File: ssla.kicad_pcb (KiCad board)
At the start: 4 copper layers, 71 x 43 mm, 56 parts, among them J101 USB_C_Receptacle_USB2.0_14P, J102 Conn_02x10_Odd_Even, J103 Conn_02x10_Odd_Even, J104 Conn_02x10_Odd_Even, J105 Conn_02x10_Odd_Even, U101 TLV75533PDRV, U102 TLV75512PDRV, U103 USBLC6-2P6, U104 CY7C68013A-56LTX, U105 ICE40HX8K-BG121, Y101 24 MHz

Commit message: 0 unrouted
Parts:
- added C15: 0.1u, Capacitor_SMD:C_0402_1005Metric, F.Cu at (136.3, 82.7)
- added C28: 0.1u, Capacitor_SMD:C_0402_1005Metric, B.Cu at (156.0, 84.8)
- added C31: 0.1u, Capacitor_SMD:C_0402_1005Metric, B.Cu at (163.1, 84.2)
- added C36: 0.1u, Capacitor_SMD:C_0402_1005Metric, B.Cu at (153.5, 83.6)
- added D1: D_TVS_Small, Diode_SMD:D_SOD-923, B.Cu at (190.9, 90.3)
- added D10: D_TVS_Small, Diode_SMD:D_SOD-923, B.Cu at (188.3, 97.9)
- added D11: D_TVS_Small, Diode_SMD:D_SOD-923, B.Cu at (183.3, 97.9)
- added D12: D_TVS_Small, Diode_SMD:D_SOD-923, B.Cu at (180.7, 97.9)
- added D13: D_TVS_Small, Diode_SMD:D_SOD-923, B.Cu at (178.2, 97.9)
- added D14: D_TVS_Small, Diode_SMD:D_SOD-923, B.Cu at (175.6, 97.9)
- added D15: D_TVS_Small, Diode_SMD:D_SOD-923, B.Cu at (170.6, 97.9)
- added D16: D_TVS_Small, Diode_SMD:D_SOD-923, B.Cu at (168.0, 97.9)
- added D17: D_TVS_Small, Diode_SMD:D_SOD-923, B.Cu at (155.9, 90.3)
- added D18: D_TVS_Small, Diode_SMD:D_SOD-923, B.Cu at (153.3, 90.3)
- added D19: D_TVS_Small, Diode_SMD:D_SOD-923, B.Cu at (148.3, 90.3)
- added D2: D_TVS_Small, Diode_SMD:D_SOD-923, B.Cu at (188.3, 90.3)
- added D20: D_TVS_Small, Diode_SMD:D_SOD-923, B.Cu at (145.7, 90.3)
- added D21: D_TVS_Small, Diode_SMD:D_SOD-923, B.Cu at (143.2, 90.3)
- added D22: D_TVS_Small, Diode_SMD:D_SOD-923, B.Cu at (140.6, 90.3)
- added D23: D_TVS_Small, Diode_SMD:D_SOD-923, B.Cu at (135.6, 90.3)
- added D24: D_TVS_Small, Diode_SMD:D_SOD-923, B.Cu at (133.0, 90.3)
- added D25: D_TVS_Small, Diode_SMD:D_SOD-923, B.Cu at (155.9, 97.9)
- added D26: D_TVS_Small, Diode_SMD:D_SOD-923, B.Cu at (153.3, 97.9)
- added D27: D_TVS_Small, Diode_SMD:D_SOD-923, B.Cu at (148.3, 97.9)
- added D28: D_TVS_Small, Diode_SMD:D_SOD-923, B.Cu at (145.7, 97.9)
- added D29: D_TVS_Small, Diode_SMD:D_SOD-923, B.Cu at (143.2, 97.9)
- added D3: D_TVS_Small, Diode_SMD:D_SOD-923, B.Cu at (183.3, 90.3)
- added D30: D_TVS_Small, Diode_SMD:D_SOD-923, B.Cu at (140.6, 97.9)
- added D31: D_TVS_Small, Diode_SMD:D_SOD-923, B.Cu at (135.6, 97.9)
- added D32: D_TVS_Small, Diode_SMD:D_SOD-923, B.Cu at (133.0, 97.9)
- added D33: D_TVS_Small, Diode_SMD:D_SOD-923, B.Cu at (155.1, 62.1)
- added D34: D_TVS_Small, Diode_SMD:D_SOD-923, B.Cu at (152.5, 62.1)
- added D35: D_TVS_Small, Diode_SMD:D_SOD-923, B.Cu at (147.5, 62.1)
- added D36: D_TVS_Small, Diode_SMD:D_SOD-923, B.Cu at (144.9, 62.1)
- added D37: D_TVS_Small, Diode_SMD:D_SOD-923, B.Cu at (142.4, 62.1)
- added D38: D_TVS_Small, Diode_SMD:D_SOD-923, B.Cu at (139.8, 62.1)
- added D39: D_TVS_Small, Diode_SMD:D_SOD-923, B.Cu at (134.8, 62.1)
- added D4: D_TVS_Small, Diode_SMD:D_SOD-923, B.Cu at (180.7, 90.3)
- added D40: D_TVS_Small, Diode_SMD:D_SOD-923, B.Cu at (132.2, 62.1)
- added D41: D_TVS_Small, Diode_SMD:D_SOD-923, B.Cu at (155.1, 69.7)
- added D42: D_TVS_Small, Diode_SMD:D_SOD-923, B.Cu at (152.5, 69.7)
- added D43: D_TVS_Small, Diode_SMD:D_SOD-923, B.Cu at (147.5, 69.7)
- added D44: D_TVS_Small, Diode_SMD:D_SOD-923, B.Cu at (144.9, 69.7)
- added D45: D_TVS_Small, Diode_SMD:D_SOD-923, B.Cu at (142.4, 69.7)
- added D46: D_TVS_Small, Diode_SMD:D_SOD-923, B.Cu at (139.8, 69.7)
- added D47: D_TVS_Small, Diode_SMD:D_SOD-923, B.Cu at (134.8, 69.7)
- added D48: D_TVS_Small, Diode_SMD:D_SOD-923, B.Cu at (132.2, 69.7)
- added D49: D_TVS_Small, Diode_SMD:D_SOD-923, B.Cu at (190.1, 62.1)
- added D5: D_TVS_Small, Diode_SMD:D_SOD-923, B.Cu at (178.2, 90.3)
- added D50: D_TVS_Small, Diode_SMD:D_SOD-923, B.Cu at (187.5, 62.1)
- added D51: D_TVS_Small, Diode_SMD:D_SOD-923, B.Cu at (182.5, 62.1)
- added D52: D_TVS_Small, Diode_SMD:D_SOD-923, B.Cu at (179.9, 62.1)
- added D53: D_TVS_Small, Diode_SMD:D_SOD-923, B.Cu at (177.4, 62.1)
- added D54: D_TVS_Small, Diode_SMD:D_SOD-923, B.Cu at (174.8, 62.1)
- added D55: D_TVS_Small, Diode_SMD:D_SOD-923, B.Cu at (169.8, 62.1)
- added D56: D_TVS_Small, Diode_SMD:D_SOD-923, B.Cu at (167.2, 62.1)
- added D57: D_TVS_Small, Diode_SMD:D_SOD-923, B.Cu at (190.1, 69.7)
- added D58: D_TVS_Small, Diode_SMD:D_SOD-923, B.Cu at (187.5, 69.7)
- added D59: D_TVS_Small, Diode_SMD:D_SOD-923, B.Cu at (182.5, 69.7)
- added D6: D_TVS_Small, Diode_SMD:D_SOD-923, B.Cu at (175.6, 90.3)
- added D60: D_TVS_Small, Diode_SMD:D_SOD-923, B.Cu at (179.9, 69.7)
- added D61: D_TVS_Small, Diode_SMD:D_SOD-923, B.Cu at (177.4, 69.7)
- added D62: D_TVS_Small, Diode_SMD:D_SOD-923, B.Cu at (174.8, 69.7)
- added D63: D_TVS_Small, Diode_SMD:D_SOD-923, B.Cu at (169.8, 69.7)
- added D64: D_TVS_Small, Diode_SMD:D_SOD-923, B.Cu at (167.2, 69.7)
- added D7: D_TVS_Small, Diode_SMD:D_SOD-923, B.Cu at (170.6, 90.3)
- added D8: D_TVS_Small, Diode_SMD:D_SOD-923, B.Cu at (168.0, 90.3)
- added D9: D_TVS_Small, Diode_SMD:D_SOD-923, B.Cu at (190.9, 97.9)
- added J6: Conn_ARM_JTAG_SWD_10, Connector_PinHeader_1.27mm:PinHeader_2x05_P1.27mm_Vertical_SMD, F.Cu at (174.0, 80.0)
- added R10: 10k, Resistor_SMD:R_0402_1005Metric, B.Cu at (149.9, 80.4)
- added R11: 100, Resistor_SMD:R_0402_1005Metric, B.Cu at (190.6, 91.7)
- added R12: 100, Resistor_SMD:R_0402_1005Metric, B.Cu at (188.0, 91.7)
- added R13: 100, Resistor_SMD:R_0402_1005Metric, B.Cu at (182.9, 91.7)
- added R14: 100, Resistor_SMD:R_0402_1005Metric, B.Cu at (180.4, 91.7)
- added R15: 100, Resistor_SMD:R_0402_1005Metric, B.Cu at (177.9, 91.7)
- added R16: 100, Resistor_SMD:R_0402_1005Metric, B.Cu at (175.3, 91.7)
- added R17: 100, Resistor_SMD:R_0402_1005Metric, B.Cu at (170.2, 91.7)
- added R18: 100, Resistor_SMD:R_0402_1005Metric, B.Cu at (167.7, 91.7)
- added R19: 100, Resistor_SMD:R_0402_1005Metric, B.Cu at (155.6, 91.7)
- added R20: 100, Resistor_SMD:R_0402_1005Metric, B.Cu at (153.0, 91.7)
- added R21: 100, Resistor_SMD:R_0402_1005Metric, B.Cu at (147.9, 91.7)
- added R22: 100, Resistor_SMD:R_0402_1005Metric, B.Cu at (145.4, 91.7)
- added R23: 100, Resistor_SMD:R_0402_1005Metric, B.Cu at (142.9, 91.7)
- added R24: 100, Resistor_SMD:R_0402_1005Metric, B.Cu at (140.3, 91.7)
- added R25: 100, Resistor_SMD:R_0402_1005Metric, B.Cu at (135.2, 91.7)
- added R26: 100, Resistor_SMD:R_0402_1005Metric, B.Cu at (132.7, 91.7)
- added R27: 100, Resistor_SMD:R_0402_1005Metric, B.Cu at (155.4, 60.7)
- added R28: 100, Resistor_SMD:R_0402_1005Metric, B.Cu at (152.9, 60.7)
- added R29: 100, Resistor_SMD:R_0402_1005Metric, B.Cu at (147.8, 60.7)
- added R30: 100, Resistor_SMD:R_0402_1005Metric, B.Cu at (145.2, 60.7)
- added R31: 100, Resistor_SMD:R_0402_1005Metric, B.Cu at (142.7, 60.7)
- added R32: 100, Resistor_SMD:R_0402_1005Metric, B.Cu at (140.2, 60.7)
- added R33: 100, Resistor_SMD:R_0402_1005Metric, B.Cu at (135.1, 60.7)
- added R34: 100, Resistor_SMD:R_0402_1005Metric, B.Cu at (132.5, 60.7)
- added R35: 100, Resistor_SMD:R_0402_1005Metric, B.Cu at (190.4, 60.7)
- added R36: 100, Resistor_SMD:R_0402_1005Metric, B.Cu at (187.9, 60.7)
- added R37: 100, Resistor_SMD:R_0402_1005Metric, B.Cu at (182.8, 60.7)
- added R38: 100, Resistor_SMD:R_0402_1005Metric, B.Cu at (180.2, 60.7)
- added R39: 100, Resistor_SMD:R_0402_1005Metric, B.Cu at (177.7, 60.7)
- added R4: 0, Resistor_SMD:R_0402_1005Metric, F.Cu at (133.9, 87.3)
- added R40: 100, Resistor_SMD:R_0402_1005Metric, B.Cu at (175.2, 60.7)
- added R41: 100, Resistor_SMD:R_0402_1005Metric, B.Cu at (170.1, 60.7)
- added R42: 100, Resistor_SMD:R_0402_1005Metric, B.Cu at (167.5, 60.7)
- added R45: 10k, Resistor_SMD:R_0402_1005Metric, B.Cu at (151.7, 87.3)
- added R46: 100, Resistor_SMD:R_0402_1005Metric, B.Cu at (190.6, 99.3)
- added R47: 100, Resistor_SMD:R_0402_1005Metric, B.Cu at (188.0, 99.3)
- added R48: 100, Resistor_SMD:R_0402_1005Metric, B.Cu at (182.9, 99.3)
- added R49: 100, Resistor_SMD:R_0402_1005Metric, B.Cu at (180.4, 99.3)
- added R50: 100, Resistor_SMD:R_0402_1005Metric, B.Cu at (177.9, 99.3)
- added R51: 100, Resistor_SMD:R_0402_1005Metric, B.Cu at (175.3, 99.3)
- added R52: 100, Resistor_SMD:R_0402_1005Metric, B.Cu at (170.2, 99.3)
- added R53: 100, Resistor_SMD:R_0402_1005Metric, B.Cu at (167.7, 99.3)
- added R54: 100, Resistor_SMD:R_0402_1005Metric, B.Cu at (155.6, 99.3)
- added R55: 100, Resistor_SMD:R_0402_1005Metric, B.Cu at (153.0, 99.3)
- added R56: 100, Resistor_SMD:R_0402_1005Metric, B.Cu at (147.9, 99.3)
- added R57: 100, Resistor_SMD:R_0402_1005Metric, B.Cu at (145.4, 99.3)
- added R58: 100, Resistor_SMD:R_0402_1005Metric, B.Cu at (142.9, 99.3)
- added R59: 100, Resistor_SMD:R_0402_1005Metric, B.Cu at (140.3, 99.3)
- added R60: 100, Resistor_SMD:R_0402_1005Metric, B.Cu at (135.2, 99.3)
- added R61: 100, Resistor_SMD:R_0402_1005Metric, B.Cu at (132.7, 99.3)
- added R62: 100, Resistor_SMD:R_0402_1005Metric, B.Cu at (155.4, 68.3)
- added R63: 100, Resistor_SMD:R_0402_1005Metric, B.Cu at (152.9, 68.3)
- added R64: 100, Resistor_SMD:R_0402_1005Metric, B.Cu at (147.8, 68.3)
- added R65: 100, Resistor_SMD:R_0402_1005Metric, B.Cu at (145.2, 68.3)
- added R66: 100, Resistor_SMD:R_0402_1005Metric, B.Cu at (142.7, 68.3)
- added R67: 100, Resistor_SMD:R_0402_1005Metric, B.Cu at (140.2, 68.3)
- added R68: 100, Resistor_SMD:R_0402_1005Metric, B.Cu at (135.1, 68.3)
- added R69: 100, Resistor_SMD:R_0402_1005Metric, B.Cu at (132.5, 68.3)
- added R70: 100, Resistor_SMD:R_0402_1005Metric, B.Cu at (190.4, 68.3)
- added R71: 100, Resistor_SMD:R_0402_1005Metric, B.Cu at (187.9, 68.3)
- added R72: 100, Resistor_SMD:R_0402_1005Metric, B.Cu at (182.8, 68.3)
- added R73: 100, Resistor_SMD:R_0402_1005Metric, B.Cu at (180.2, 68.3)
- added R74: 100, Resistor_SMD:R_0402_1005Metric, B.Cu at (177.7, 68.3)
- added R75: 100, Resistor_SMD:R_0402_1005Metric, B.Cu at (175.2, 68.3)
- added R76: 100, Resistor_SMD:R_0402_1005Metric, B.Cu at (170.1, 68.3)
- added R77: 100, Resistor_SMD:R_0402_1005Metric, B.Cu at (167.5, 68.3)
- added R78: 10k, Resistor_SMD:R_0402_1005Metric, B.Cu at (151.7, 86.2)
- added R79: 10k, Resistor_SMD:R_0402_1005Metric, B.Cu at (153.7, 86.8)
- added R8: 100k, Resistor_SMD:R_0402_1005Metric, B.Cu at (152.1, 83.2)
- added R9: 10k, Resistor_SMD:R_0402_1005Metric, B.Cu at (150.0, 86.8)
- added TP11: TestPoint_Small, TestPoint:TestPoint_Pad_D1.0mm, B.Cu at (142.0, 81.6)
- added TP12: TestPoint_Small, TestPoint:TestPoint_Pad_D1.0mm, B.Cu at (142.1, 77.0)
- added U3: BL24C256A, Package_SO:TSSOP-8_4.4x3mm_P0.65mm, F.Cu at (134.0, 85.0)
- added U7: W25Q16JVUXIQ, Package_SON:Winbond_USON-8-1EP_3x2mm_P0.5mm_EP0.2x1.6mm, F.Cu at (154.0, 84.5)
- C1: renamed from C101; moved to B.Cu
- C10: renamed from C110; moved to B.Cu
- C13: renamed from C113; moved to B.Cu
- C14: renamed from C114; moved to B.Cu
- C2: renamed from C102; moved to B.Cu
- C23: renamed from C122; moved to B.Cu
- C24: renamed from C123; moved to B.Cu
- C25: renamed from C124; moved to B.Cu
- C32: renamed from C129; moved to B.Cu
- C33: renamed from C130; moved to B.Cu
- C34: renamed from C131; moved to B.Cu
- C35: renamed from C132; moved to B.Cu
- C5: renamed from C105; moved to B.Cu
- C6: renamed from C106; moved to B.Cu
- C9: renamed from C109; moved to B.Cu
- J2: renamed from J102; footprint Connector_PinHeader_2.54mm:PinHeader_2x10_P2.54mm_Vertical_SMD -> Connector_IDC:IDC-Header_2x10_P2.54mm_Vertical_SMD
- J3: renamed from J103; footprint Connector_PinHeader_2.54mm:PinHeader_2x10_P2.54mm_Vertical_SMD -> Connector_IDC:IDC-Header_2x10_P2.54mm_Vertical_SMD
- J4: renamed from J104; footprint Connector_PinHeader_2.54mm:PinHeader_2x10_P2.54mm_Vertical_SMD -> Connector_IDC:IDC-Header_2x10_P2.54mm_Vertical_SMD
- J5: renamed from J105; footprint Connector_PinHeader_2.54mm:PinHeader_2x10_P2.54mm_Vertical_SMD -> Connector_IDC:IDC-Header_2x10_P2.54mm_Vertical_SMD
- R1: renamed from R101; moved to B.Cu
- R2: renamed from R102; moved to B.Cu
- R43: renamed from R107; moved to B.Cu
- R44: renamed from R108; moved to B.Cu
- R6: renamed from R105; value 2.2k -> 100k; moved to B.Cu
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- renumbered C111 to C11, C112 to C12, C115 to C16, C116 to C17, C117 to C18, C118 to C19, C119 to C20, C120 to C21, C121 to C22, C125 to C26, C126 to C27, C127 to C29, C103 to C3, C128 to C30, C104 to C4, C107 to C7, C108 to C8, FB101 to FB1, H101 to H1, H102 to H2, H103 to H3, H104 to H4, J101 to J1, R103 to R3, R104 to R5, R106 to R7, U101 to U1, U102 to U2, U103 to U4, U104 to U5, U105 to U6, Y101 to Y1
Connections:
- J2 pad 1: /IO00 -> Net-(J2-Pin_1)
- J2 pad 10: /IO11 -> Net-(J2-Pin_10)
- J2 pad 11: /IO04 -> Net-(J2-Pin_11)
- J2 pad 12: /IO12 -> Net-(J2-Pin_12)
- J2 pad 13: /IO05 -> Net-(J2-Pin_13)
- J2 pad 14: /IO13 -> Net-(J2-Pin_14)
- J2 pad 17: /IO06 -> Net-(J2-Pin_17)
- J2 pad 18: /IO14 -> Net-(J2-Pin_18)
- J2 pad 19: /IO07 -> Net-(J2-Pin_19)
- J2 pad 2: /IO08 -> Net-(J2-Pin_2)
- J2 pad 20: /IO15 -> Net-(J2-Pin_20)
- J2 pad 3: /IO01 -> Net-(J2-Pin_3)
- J2 pad 4: /IO09 -> Net-(J2-Pin_4)
- J2 pad 7: /IO02 -> Net-(J2-Pin_7)
- J2 pad 8: /IO10 -> Net-(J2-Pin_8)
- J2 pad 9: /IO03 -> Net-(J2-Pin_9)
- J3 pad 1: /IO16 -> Net-(J3-Pin_1)
- J3 pad 10: /IO27 -> Net-(J3-Pin_10)
- J3 pad 11: /IO20 -> Net-(J3-Pin_11)
- J3 pad 12: /IO28 -> Net-(J3-Pin_12)
- J3 pad 13: /IO21 -> Net-(J3-Pin_13)
- J3 pad 14: /IO29 -> Net-(J3-Pin_14)
- J3 pad 17: /IO22 -> Net-(J3-Pin_17)
- J3 pad 18: /IO30 -> Net-(J3-Pin_18)
- J3 pad 19: /IO23 -> Net-(J3-Pin_19)
- J3 pad 2: /IO24 -> Net-(J3-Pin_2)
- J3 pad 20: /IO31 -> Net-(J3-Pin_20)
- J3 pad 3: /IO17 -> Net-(J3-Pin_3)
- J3 pad 4: /IO25 -> Net-(J3-Pin_4)
- J3 pad 7: /IO18 -> Net-(J3-Pin_7)
- J3 pad 8: /IO26 -> Net-(J3-Pin_8)
- J3 pad 9: /IO19 -> Net-(J3-Pin_9)
- J4 pad 1: /IO32 -> Net-(J4-Pin_1)
- J4 pad 10: /IO43 -> Net-(J4-Pin_10)
- J4 pad 11: /IO36 -> Net-(J4-Pin_11)
- J4 pad 12: /IO44 -> Net-(J4-Pin_12)
- J4 pad 13: /IO37 -> Net-(J4-Pin_13)
- J4 pad 14: /IO45 -> Net-(J4-Pin_14)
- J4 pad 17: /IO38 -> Net-(J4-Pin_17)
- J4 pad 18: /IO46 -> Net-(J4-Pin_18)
- J4 pad 19: /IO39 -> Net-(J4-Pin_19)
- J4 pad 2: /IO40 -> Net-(J4-Pin_2)
- J4 pad 20: /IO47 -> Net-(J4-Pin_20)
- J4 pad 3: /IO33 -> Net-(J4-Pin_3)
- J4 pad 4: /IO41 -> Net-(J4-Pin_4)
- J4 pad 7: /IO34 -> Net-(J4-Pin_7)
- J4 pad 8: /IO42 -> Net-(J4-Pin_8)
- J4 pad 9: /IO35 -> Net-(J4-Pin_9)
- J5 pad 1: /IO48 -> Net-(J5-Pin_1)
- J5 pad 10: /IO59 -> Net-(J5-Pin_10)
- J5 pad 11: /IO52 -> Net-(J5-Pin_11)
- J5 pad 12: /IO60 -> Net-(J5-Pin_12)
- J5 pad 13: /IO53 -> Net-(J5-Pin_13)
- J5 pad 14: /IO61 -> Net-(J5-Pin_14)
- J5 pad 17: /IO54 -> Net-(J5-Pin_17)
- J5 pad 18: /IO62 -> Net-(J5-Pin_18)
- J5 pad 19: /IO55 -> Net-(J5-Pin_19)
- J5 pad 2: /IO56 -> Net-(J5-Pin_2)
- J5 pad 20: /IO63 -> Net-(J5-Pin_20)
- J5 pad 3: /IO49 -> Net-(J5-Pin_3)
- J5 pad 4: /IO57 -> Net-(J5-Pin_4)
- J5 pad 7: /IO50 -> Net-(J5-Pin_7)
- J5 pad 8: /IO58 -> Net-(J5-Pin_8)
- J5 pad 9: /IO51 -> Net-(J5-Pin_9)
- U5 pad 31: /CTL2/FLAGC -> unconnected-(U5-CTL2/FLAGC-Pad31)
- U5 pad 34: /PA1/~{INT1} -> /~{CRESET}
- U5 pad 36: /PA3/WU2 -> /CDONE
- U5 pad 40: /PA7/FLAGD/~{SLCS} -> unconnected-(U5-PA7/FLAGD/~{SLCS}-Pad40)
- U5 pad 45: /PD0/FD8 -> unconnected-(U5-PD0/FD8-Pad45)
- U5 pad 46: /PD1/FD9 -> unconnected-(U5-PD1/FD9-Pad46)
- U5 pad 47: /PD2/FD10 -> unconnected-(U5-PD2/FD10-Pad47)
- U5 pad 48: /PD3/FD11 -> unconnected-(U5-PD3/FD11-Pad48)
- U5 pad 49: /PD4/FD12 -> unconnected-(U5-PD4/FD12-Pad49)
- U5 pad 50: /PD5/FD13 -> unconnected-(U5-PD5/FD13-Pad50)
- U5 pad 51: /PD6/FD14 -> unconnected-(U5-PD6/FD14-Pad51)
- U5 pad 52: /PD7/FD15 -> unconnected-(U5-PD7/FD15-Pad52)
- U6 pad A1: /IO22 -> /IO59
- U6 pad A10: /IO01 -> /IO07
- U6 pad A11: /IO00 -> /IO12
- U6 pad A2: /IO20 -> /IO50
- U6 pad A3: /IO21 -> /IO49
- U6 pad A4: /IO16 -> /IO48
- U6 pad A5: /IO14 -> /IO00
- U6 pad A6: /IO13 -> /IO01
- U6 pad A7: /IO10 -> /IO02
- U6 pad A8: /IO08 -> /IO03
- U6 pad B1: /IO44 -> /IO60
- U6 pad B11: /IO43 -> /IO13
- U6 pad B2: /IO45 -> /IO51
- U6 pad B3: /IO19 -> /IO57
- U6 pad B4: /IO18 -> /IO56
- U6 pad B5: /IO15 -> /IO08
- U6 pad B6: /IO12 -> unconnected-(U6A-IOT_198_GBIN0-PadB6)
- U6 pad B7: /IO11 -> unconnected-(U6A-IOT_197_GBIN1-PadB7)
- U6 pad B9: /IO03 -> /IO06
- U6 pad C1: /IO49 -> /IO61
- U6 pad C11: /IO42 -> /IO14
- U6 pad C2: /IO48 -> /IO52
- U6 pad C3: /IO47 -> /IO58
- U6 pad C4: /IO46 -> /IO42
- U6 pad C7: /IO09 -> /IO10
- U6 pad C8: /IO06 -> /IO62
- U6 pad C9: /IO02 -> /IO11
- U6 pad D1: /IO51 -> /IO54
- U6 pad D10: /IO41 -> /IO30
- U6 pad D11: /IO40 -> /IO29
- U6 pad D2: /IO52 -> /IO53
- U6 pad D3: /IO53 -> /IO43
- U6 pad D5: /IO17 -> /IO63
- U6 pad D7: /IO07 -> /IO09
- U6 pad D9: /IO38 -> /IO15
- U6 pad E1: /IO50 -> /IO32
- U6 pad E10: /IO35 -> unconnected-(U6B-IOR_141_GBIN2-PadE10)
- U6 pad E11: /IO39 -> /IO31
- U6 pad E2: /IO54 -> /IO55
- U6 pad E3: /IO55 -> /IO44
- U6 pad E8: /IO37 -> /IO17
- U6 pad E9: /IO36 -> /IO16
- U6 pad F1: /IO56 -> /IO34
- U6 pad F10: /IO32 -> /IO22
- U6 pad F11: /IO34 -> unconnected-(U6B-IOR_140_GBIN3-PadF11)
- U6 pad F2: /IO57 -> /IO33
- U6 pad F3: /IO59 -> unconnected-(U6D-IOL_13B_GBIN7-PadF3)
- U6 pad F4: /IO58 -> /IO45
- U6 pad F9: /IO33 -> /IO23
- U6 pad G1: /IO60 -> unconnected-(U6D-IOL_14A_GBIN6-PadG1)
- U6 pad G10: /IO29 -> /IO25
- U6 pad G11: /IO31 -> /IO24
- U6 pad G2: /IO61 -> /IO35
- U6 pad G3: /IO62 -> /IO46
- U6 pad G8: /IO27 -> /IO18
- U6 pad G9: /IO30 -> /IO19
- U6 pad H1: unconnected-(U105D-IOL_18A-PadH1) -> /IO40
- U6 pad H10: /IO25 -> /IO27
- U6 pad H11: /IO28 -> /IO26
- U6 pad H2: unconnected-(U105D-IOL_18B-PadH2) -> /IO36
- U6 pad H3: /IO63 -> /IO47
- U6 pad H7: /RDY0/SLRD -> /CTL0/FLAGA
- U6 pad H9: /PB7/FD7 -> /CTL1/FLAGB
- U6 pad J1: unconnected-(U105D-IOL_23A-PadJ1) -> /IO37
- U6 pad J10: /IO26 -> /IO20
- U6 pad J11: /IO23 -> /IO28
- U6 pad J2: unconnected-(U105D-IOL_25B-PadJ2) -> /IO41
- U6 pad J3: unconnected-(U105C-IOB_57-PadJ3) -> /PA5/FIOADDR1
- U6 pad J4: unconnected-(U105C-IOB_64-PadJ4) -> /PA6/PKTEND
- U6 pad J5: unconnected-(U105C-IOB_78-PadJ5) -> /PA4/FIOADDR0
- U6 pad J7: unconnected-(U105C-IOB_86-PadJ7) -> /PA0/~{INT0}
- U6 pad J8: /PB4/FD4 -> /PA2/SLOE
- U6 pad J9: /PB1/FD1 -> /IOB_106_SDI
- U6 pad K1: unconnected-(U105D-IOL_23B-PadK1) -> /IO39
- U6 pad K10: /PB3/FD3 -> /IOB_108_SS
- U6 pad K11: /IO24 -> /IO21
- U6 pad K2: unconnected-(U105D-IOL_25A-PadK2) -> /IO38
- U6 pad K3: unconnected-(U105C-IOB_63-PadK3) -> /PB7/FD7
- U6 pad K4: unconnected-(U105C-IOB_73-PadK4) -> /PB5/FD5
- U6 pad K5: unconnected-(U105C-IOB_79-PadK5) -> /PB3/FD3
- U6 pad K6: /CLKOUT -> /IFCLK
- U6 pad K7: /RDY1/SLWR -> /PB1/FD1
- U6 pad K8: unconnected-(U105C-CDONE-PadK8) -> /CDONE
- U6 pad K9: /PB0/FD0 -> /IOB_105_SDO
- U6 pad L1: unconnected-(U105C-IOB_56-PadL1) -> /RDY1/SLWR
- U6 pad L10: /PB2/FD2 -> /IOB_107_SCK
- U6 pad L2: unconnected-(U105C-IOB_61-PadL2) -> /RDY0/SLRD
- U6 pad L3: unconnected-(U105C-IOB_71-PadL3) -> /PB6/FD6
- U6 pad L4: unconnected-(U105C-IOB_72-PadL4) -> /PB4/FD4
- U6 pad L5: /IFCLK -> /CLKOUT
- U6 pad L7: /PB5/FD5 -> /PB2/FD2
- U6 pad L8: /PB6/FD6 -> /PB0/FD0
- U6 pad L9: unconnected-(U105C-~{CRESET}-PadL9) -> /~{CRESET}
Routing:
- net +3V3: track 22.2 -> 142.7 mm, vias 18 -> 22
- net +1V2: track 4.20 -> 94.2 mm, vias 6 -> 8
- net GND: track 40.7 -> 107.3 mm, vias 39 -> 179
- net /~{CRESET}: track 0.00 -> 53.8 mm, vias 0 -> 5
- net /IO23: track 0.90 -> 46.9 mm, vias 0 -> 1
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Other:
- board size 71 x 43 mm -> 81 x 51 mm
- board text added: "3.3V GND GND GND"
- board text added: "CS SCK MOSI MISO RST"
- board text added: "Vortessence"

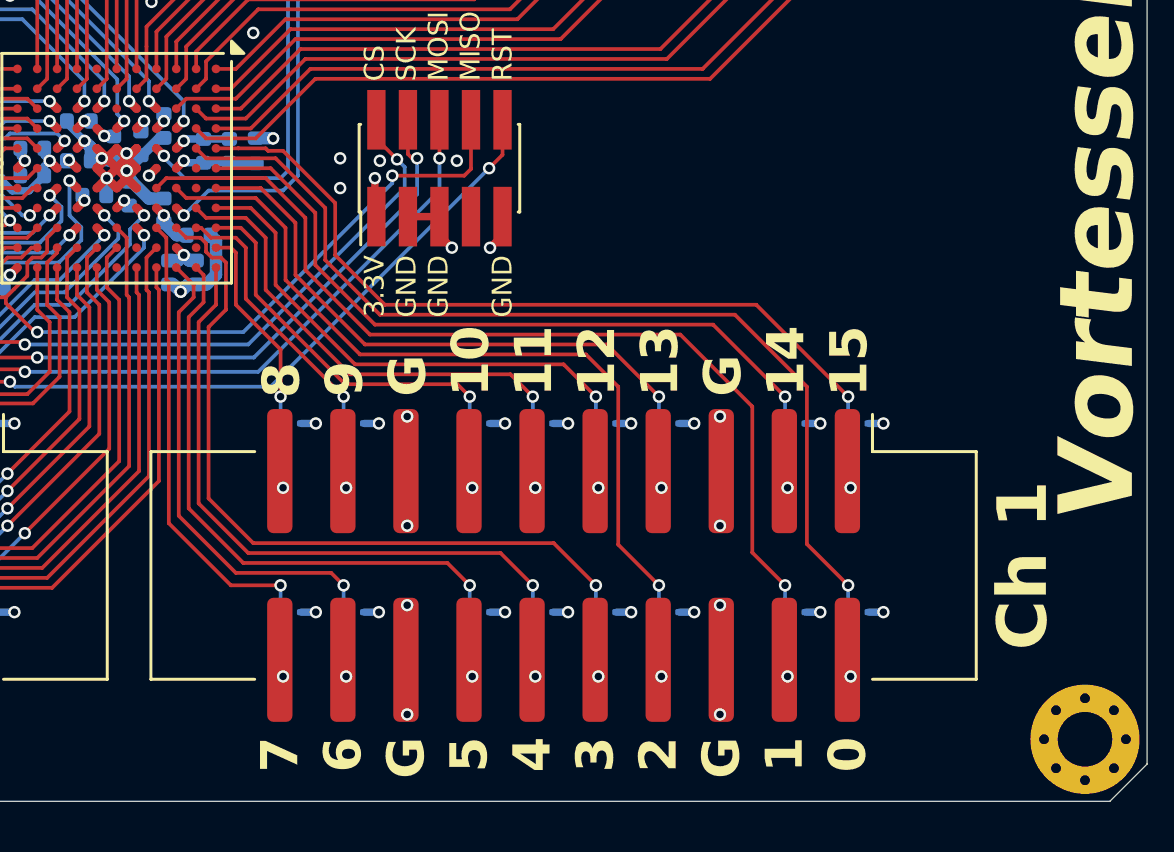
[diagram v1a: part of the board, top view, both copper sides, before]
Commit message: LCSC part numbers, started moving to through-hole IDC connector
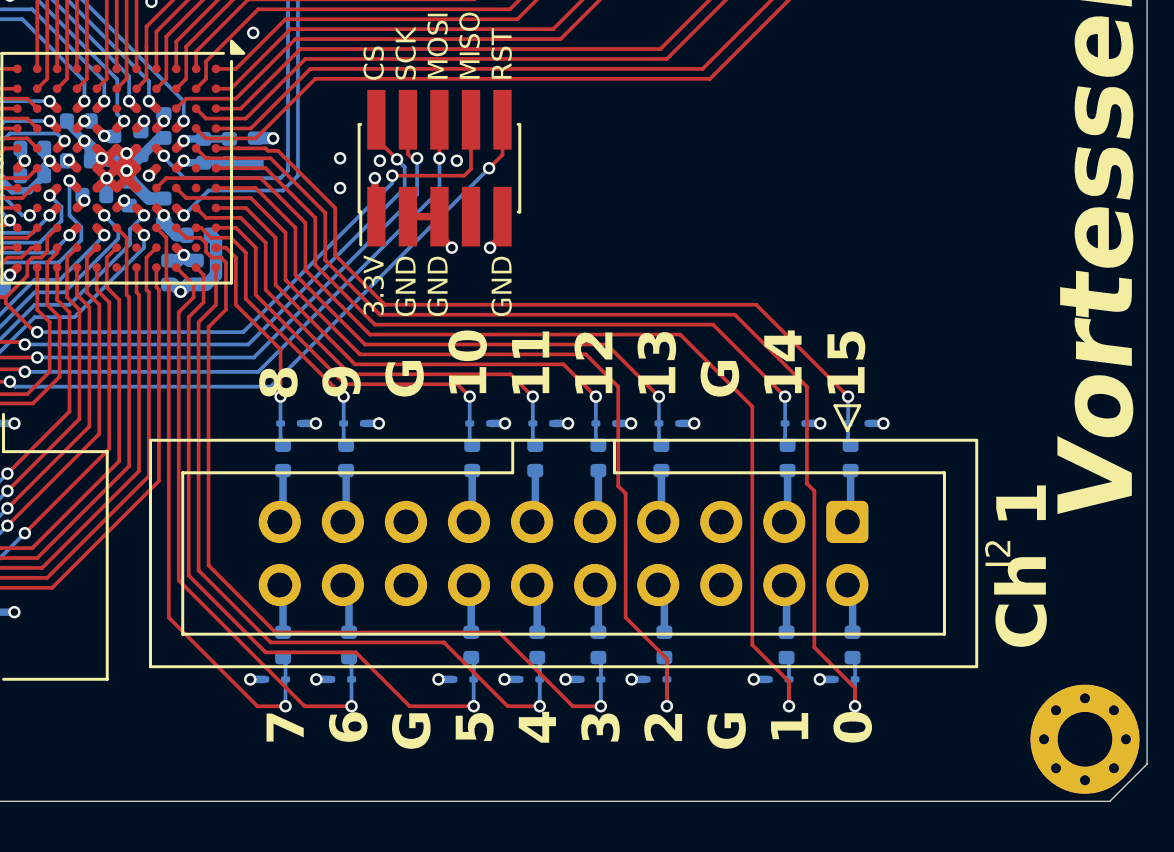
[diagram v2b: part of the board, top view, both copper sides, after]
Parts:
- C19, C20: value 10p -> 12p
- J2: footprint Connector_IDC:IDC-Header_2x10_P2.54mm_Vertical_SMD -> Connector_IDC:IDC-Header_2x10_P2.54mm_Vertical
- moved J2 11.6 mm to (190.4, 94.2)
- moved D10 2.79 mm to (187.7, 100.6), turned to 0 degrees
- moved D14 2.79 mm to (175.0, 100.6), turned to 0 degrees
- moved D16 2.78 mm to (167.4, 100.6), turned to 0 degrees
- moved D12 2.78 mm to (180.1, 100.6), turned to 0 degrees
- moved D13 2.77 mm to (177.6, 100.6), turned to 0 degrees
- moved D9 2.77 mm to (190.3, 100.6), turned to 0 degrees
- moved D15 2.76 mm to (170.0, 100.6), turned to 0 degrees
- moved D11 2.76 mm to (182.7, 100.6), turned to 0 degrees
- moved R48 0.14 mm to (183.1, 99.2), turned to -90 degrees
- moved R52 0.14 mm to (170.4, 99.2), turned to -90 degrees
- moved R46 0.11 mm to (190.6, 99.2), turned to -90 degrees
- moved R50 0.11 mm to (177.9, 99.2), turned to -90 degrees
- moved R47 0.08 mm to (188.0, 99.2), turned to -90 degrees
- moved R51 0.08 mm to (175.3, 99.2), turned to -90 degrees
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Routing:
- net /IO10: track 33.1 -> 38.0 mm
- net /IO08: track 40.6 -> 45.4 mm
- net /IO09: track 39.0 -> 43.8 mm
- net /IO15: track 19.7 -> 24.1 mm
- net /IO12: track 26.7 -> 30.6 mm
- net /IO14: track 20.4 -> 24.3 mm
- net /IO11: track 31.7 -> 35.5 mm
- net /IO13: track 24.7 -> 28.5 mm
- net Net-(J2-Pin_3): track 0.69 -> 2.12 mm, vias 1 -> 0
- net Net-(J2-Pin_11): track 0.69 -> 2.12 mm, vias 1 -> 0
- net Net-(J2-Pin_9): track 0.69 -> 2.12 mm, vias 1 -> 0
- net Net-(J2-Pin_19): track 0.69 -> 2.12 mm, vias 1 -> 0
- net Net-(J2-Pin_13): track 0.69 -> 2.12 mm, vias 1 -> 0
- net Net-(J2-Pin_1): track 0.69 -> 2.12 mm, vias 1 -> 0
- net Net-(J2-Pin_7): track 0.69 -> 2.12 mm, vias 1 -> 0
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
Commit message: Save
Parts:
- J3, J4, J5: footprint Connector_IDC:IDC-Header_2x10_P2.54mm_Vertical_SMD -> Connector_IDC:IDC-Header_2x10_P2.54mm_Vertical
- moved J3 11.6 mm to (155.4, 94.2)
- moved J4 11.5 mm to (155.4, 63.2)
- moved J5 11.5 mm to (190.4, 63.2)
- moved D49 3.26 mm to (190.1, 58.9), turned to 180 degrees
- moved D50 3.26 mm to (187.5, 58.9), turned to 180 degrees
- moved D51 3.26 mm to (182.5, 58.9), turned to 180 degrees
- moved D52 3.26 mm to (179.9, 58.9), turned to 180 degrees
- moved D53 3.26 mm to (177.4, 58.9), turned to 180 degrees
- moved D54 3.26 mm to (174.8, 58.9), turned to 180 degrees
- moved D55 3.26 mm to (169.8, 58.9), turned to 180 degrees
- moved D56 3.26 mm to (167.2, 58.9), turned to 180 degrees
- moved D28 2.90 mm to (144.7, 100.6), turned to 0 degrees
- moved D29 2.88 mm to (142.2, 100.6), turned to 0 degrees
- moved D30 2.85 mm to (139.8, 100.6), turned to 0 degrees
- moved D31 2.80 mm to (134.8, 100.6), turned to 0 degrees
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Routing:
- net /IO36: track 30.0 -> 15.5 mm
- net /IO35: track 28.1 -> 16.1 mm
- net /IO34: track 25.1 -> 15.6 mm
- net /IO49: track 35.1 -> 26.8 mm
- net /IO52: track 26.9 -> 18.7 mm
- net /IO51: track 28.3 -> 20.1 mm
- net /IO50: track 29.6 -> 21.4 mm
- net /IO48: track 37.9 -> 29.7 mm
- net /IO53: track 25.4 -> 17.2 mm
- net /IO39: track 37.5 -> 29.6 mm
- net /IO37: track 30.9 -> 23.0 mm
- net /IO38: track 36.7 -> 29.0 mm
- net /IO54: track 19.4 -> 12.0 mm
- net /IO55: track 18.3 -> 11.0 mm
- net /IO27: track 25.3 -> 31.9 mm
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
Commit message: Save
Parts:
- moved H1 1.00 mm to (200.0, 102.0)
- moved H2 1.00 mm to (200.0, 58.0)
- moved H3 1.00 mm to (124.0, 102.0)
- moved H4 1.00 mm to (124.0, 58.0)
- moved D36 0.79 mm to (145.5, 59.3)
- moved D39 0.79 mm to (135.4, 59.3)
- moved R27 0.79 mm to (155.4, 60.7)
- moved R29 0.79 mm to (147.7, 60.7)
- moved D33 0.79 mm to (155.7, 59.3)
- moved D34 0.79 mm to (153.1, 59.3)
- moved D35 0.79 mm to (148.1, 59.3)
- moved D37 0.79 mm to (143.0, 59.3)
- moved D38 0.79 mm to (140.4, 59.3)
- moved D40 0.79 mm to (132.8, 59.3)
- moved R28 0.79 mm to (152.8, 60.7)
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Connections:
- U6 pad G10: /IO25 -> /IO27
- U6 pad G11: /IO24 -> /IO28
- U6 pad H10: /IO27 -> /IO25
- U6 pad J11: /IO28 -> /IO24
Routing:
- net /IO36: track 15.5 -> 32.7 mm
- net /IO35: track 16.1 -> 30.8 mm
- net /IO34: track 15.6 -> 27.8 mm
- net /IO51: track 20.1 -> 31.4 mm
- net /IO50: track 21.4 -> 32.6 mm
- net /IO49: track 26.8 -> 38.0 mm
- net /IO48: track 29.7 -> 40.9 mm
- net /IO52: track 18.7 -> 29.8 mm
- net /IO39: track 29.6 -> 40.4 mm
- net /IO37: track 23.0 -> 33.7 mm
- net /IO55: track 11.0 -> 21.4 mm
- net /IO38: track 29.0 -> 39.3 mm
- net /IO54: track 12.0 -> 21.3 mm
- net /IO53: track 17.2 -> 26.1 mm
- net /IO33: track 17.0 -> 24.2 mm
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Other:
- board size 81 x 51 mm -> 81 x 49 mm
- board text added: "VORTESSENCE"
- board text removed: "Vortessence"

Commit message: Started move to ECP5
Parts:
- added C37: 10n, Capacitor_SMD:C_0402_1005Metric, B.Cu at (153.9, 82.8)
- added C38: 0.1u, Capacitor_SMD:C_0402_1005Metric, B.Cu at (159.5, 83.9)
- added C39: 10n, Capacitor_SMD:C_0402_1005Metric, B.Cu at (154.5, 78.5)
- added C40: 0.1u, Capacitor_SMD:C_0402_1005Metric, B.Cu at (153.5, 78.5)
- added C41: 10n, Capacitor_SMD:C_0402_1005Metric, B.Cu at (155.8, 82.8)
- added C42: 0.1u, Capacitor_SMD:C_0402_1005Metric, B.Cu at (157.5, 78.5)
- added C43: 10n, Capacitor_SMD:C_0402_1005Metric, B.Cu at (157.7, 76.9)
- added C44: 0.1u, Capacitor_SMD:C_0402_1005Metric, B.Cu at (159.1, 77.3)
- added C45: 10n, Capacitor_SMD:C_0402_1005Metric, B.Cu at (160.8, 77.5)
- added D65: LED_Small, LED_SMD:LED_0603_1608Metric, F.Cu at (167.5, 77.0)
- added L1: 1.5u, Inductor_SMD:L_1008_2520Metric, F.Cu at (162.6, 133.1)
- added R80: 10k, Resistor_SMD:R_0402_1005Metric, B.Cu at (163.1, 80.4)
- added R81: 82k, Resistor_SMD:R_0402_1005Metric, F.Cu at (183.3, 119.1)
- added R82: 100k, Resistor_SMD:R_0402_1005Metric, F.Cu at (183.3, 121.1)
- added U8: TPS62A01ADRLR, Package_TO_SOT_SMD:SOT-563, F.Cu at (167.0, 132.9)
- C1: value 4.7u -> 10n
- C10, C14, C5, C9: value 0.1u -> 10n
- C16, C4: value 4.7u -> 0.1u; moved to B.Cu
- C17: value 4.7u -> 10n; moved to B.Cu
- C2, C35: value 4.7u -> 0.1u
- C23, C24: value 0.1u -> 4.7u; moved to F.Cu
- C28, C31, C33: value 0.1u -> 10u; footprint Capacitor_SMD:C_0402_1005Metric -> Capacitor_SMD:C_0603_1608Metric; moved to F.Cu
- C32: value 0.1u -> 27p; moved to F.Cu
- C34: value 4.7u -> 10u; footprint Capacitor_SMD:C_0402_1005Metric -> Capacitor_SMD:C_0603_1608Metric; moved to F.Cu
- C7: moved to B.Cu
- J6: value Conn_ARM_JTAG_SWD_10 -> TC2050; footprint Connector_PinHeader_1.27mm:PinHeader_2x05_P1.27mm_Vertical_SMD -> Connector:Tag-Connect_TC2050-IDC-NL_2x05_P1.27mm_Vertical
- R10, R9: value 10k -> 1k
- R3: value 100k -> 1k; moved to B.Cu
- R4: footprint Resistor_SMD:R_0402_1005Metric -> Resistor_SMD:R_0805_2012Metric
- R43: value 100 -> 1k; moved to F.Cu
- R44: value 100 -> 1k
- U2: value TLV75512PDRV -> AP2127K-2.5; footprint Package_SON:WSON-6-1EP_2x2mm_P0.65mm_EP1x1.6mm -> Package_TO_SOT_SMD:SOT-23-5
- U6: value ICE40HX8K-BG121 -> ECP5U_25_CABGA256; footprint Package_BGA:BGA-121_9.0x9.0mm_Layout11x11_P0.8mm_Ball0.4mm_Pad0.35mm_NSMD -> Package_BGA:BGA-256_14.0x14.0mm_Layout16x16_P0.8mm_Ball0.45mm_Pad0.32mm_NSMD
- moved U2 57.4 mm to (157.6, 133.6), turned to 0 degrees
- moved C32 54.6 mm to (182.1, 129.1), turned to 0 degrees
- moved C24 52.5 mm to (182.1, 127.2), turned to 0 degrees
- moved C23 50.8 mm to (182.1, 125.2)
- moved C34 46.7 mm to (174.1, 122.9), turned to 0 degrees
- moved C33 42.2 mm to (174.1, 120.4), turned to 0 degrees
- moved R3 37.7 mm to (164.4, 78.5), turned to 0 degrees
- moved C28 35.5 mm to (174.1, 115.4), turned to 0 degrees
- moved C31 35.5 mm to (174.1, 117.9), turned to 0 degrees
- moved C4 33.8 mm to (157.7, 82.8), turned to 90 degrees
- moved C16 30.4 mm to (155.0, 80.4), turned to -90 degrees
- moved C7 28.7 mm to (156.0, 78.2), turned to 135 degrees
- moved C17 28.4 mm to (154.0, 80.4), turned to -90 degrees
- moved R4 18.6 mm to (146.5, 73.6)
- moved R9 15.9 mm to (165.7, 84.2), turned to -90 degrees
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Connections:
- C1 pad 1: +3V3 -> GND
- C1 pad 2: GND -> +3V3
- C10 pad 1: +1V2 -> GND
- C10 pad 2: GND -> +2V5
- C13 pad 1: +3V3 -> GND
- C13 pad 2: GND -> +1V1
- C14 pad 1: +1V2 -> GND
- C14 pad 2: GND -> +1V1
- C16 pad 1: +3V3 -> GND
- C16 pad 2: GND -> +1V1
- C17 pad 1: +1V2 -> GND
- C17 pad 2: GND -> +1V1
- C2 pad 1: +1V2 -> GND
- C2 pad 2: GND -> +3V3
- C23 pad 1: +3V3 -> +5V
- C24 pad 1: +1V2 -> +5V
- C28 pad 1: +3V3 -> +2V5
- C32 pad 1: Net-(U6E-VCCPLL0) -> /FB
- C32 pad 2: Net-(U6E-GNDPLL0) -> +1V1
- C33 pad 1: Net-(U6E-VCCPLL1) -> +1V1
- C33 pad 2: Net-(U6E-GNDPLL1) -> GND
- C34 pad 1: Net-(U6E-VCCPLL0) -> +1V1
- C34 pad 2: Net-(U6E-GNDPLL0) -> GND
- C35 pad 1: Net-(U6E-VCCPLL1) -> GND
- C35 pad 2: Net-(U6E-GNDPLL1) -> +3V3
- C4 pad 1: +5V -> GND
- C4 pad 2: GND -> +3V3
- C5 pad 1: +3V3 -> GND
- C5 pad 2: GND -> +3V3
- C6 pad 1: +1V2 -> GND
- C6 pad 2: GND -> +1V1
- C7 pad 1: /3V3_EN -> GND
- C7 pad 2: GND -> +2V5
- C9 pad 1: +3V3 -> GND
- C9 pad 2: GND -> +1V1
- J6 pad 10: /~{CRESET} -> unconnected-(J6-Pin_10-Pad10)
- J6 pad 2: /IOB_108_SS -> /TMS
- J6 pad 4: /IOB_107_SCK -> /TCK
- J6 pad 5: GND -> unconnected-(J6-Pin_5-Pad5)
- J6 pad 6: /IOB_105_SDO -> /TDO
- J6 pad 8: /IOB_106_SDI -> /TDI
- J6 pad 9: GND -> unconnected-(J6-Pin_9-Pad9)
- R10 pad 1: /CDONE -> /CFG_1
- R3 pad 1: +1V2 -> GND
- R3 pad 2: /3V3_EN -> /TCK
- R43 pad 1: +1V2 -> Net-(D65-A)
- R43 pad 2: Net-(U6E-VCCPLL0) -> +3V3
- R44 pad 1: +1V2 -> /PROGRAMN
- R44 pad 2: Net-(U6E-VCCPLL1) -> +3V3
- R45 pad 1: /IOB_108_SS -> /SPI_CS
- R78 pad 1: Net-(U7-IO3) -> /SPI_D3
- R79 pad 1: Net-(U7-IO2) -> /SPI_D2
- R9 pad 1: /~{CRESET} -> /SPI_CLK
- U1 pad 4: /3V3_EN -> +5V
- U2 pad 1: +1V2 -> +5V
- U2 pad 2: unconnected-(U2-NC-Pad2) -> GND
- U2 pad 3: GND -> +5V
- U2 pad 4: +5V -> unconnected-(U2-NC-Pad4)
- U2 pad 5: unconnected-(U2-NC-Pad5) -> +2V5
- U6 pad A1: /IO59 -> GND
- U6 pad A10: /IO07 -> /PB7/FD7
- U6 pad A11: /IO12 -> /PB1/FD1
- U6 pad A2: /IO50 -> unconnected-(U6B-PT4A/+-PadA2)
- U6 pad A3: /IO49 -> unconnected-(U6B-PT6A/+-PadA3)
- U6 pad A4: /IO48 -> unconnected-(U6B-PT6B/--PadA4)
- U6 pad A5: /IO00 -> unconnected-(U6B-PT18A/+-PadA5)
- U6 pad A6: /IO01 -> unconnected-(U6B-PT18B/--PadA6)
- U6 pad A7: /IO02 -> unconnected-(U6B-PT29A/+/PCLKT0_0-PadA7)
- U6 pad A8: /IO03 -> unconnected-(U6B-PT29B/-/PCLKC0_0-PadA8)
- U6 pad A9: /IO05 -> /RDY0/SLRD
- U6 pad B1: /IO60 -> /IO16
- U6 pad B10: unconnected-(U6E-VPP_FAST-PadB10) -> /PA6/PKTEND
- U6 pad B11: /IO13 -> /PA4/FIOADDR0
- U6 pad B2: /IO51 -> /IO17
- U6 pad B3: /IO57 -> unconnected-(U6B-PT4B/--PadB3)
- U6 pad B4: /IO56 -> unconnected-(U6B-PT11B/--PadB4)
- U6 pad B5: /IO08 -> unconnected-(U6B-PT15B/--PadB5)
- U6 pad B8: /IO04 -> unconnected-(U6C-PT35B/-/PCLKC1_0-PadB8)
- U6 pad B9: /IO06 -> /CLKOUT
- U6 pad C1: /IO61 -> /IO18
- U6 pad C10: +3V3 -> /PB6/FD6
- U6 pad C11: /IO14 -> unconnected-(U6C-PT49B/--PadC11)
- U6 pad C2: /IO52 -> /IO19
- U6 pad C3: /IO58 -> unconnected-(U6G-PL2C/+/LDQ8-PadC3)
- U6 pad C4: /IO42 -> unconnected-(U6B-PT11A/+-PadC4)
- U6 pad C5: Net-(U6E-GNDPLL1) -> unconnected-(U6B-PT15A/+-PadC5)
- U6 pad C6: Net-(U6E-VCCPLL1) -> unconnected-(U6B-PT22A/+-PadC6)
- U6 pad C7: /IO10 -> unconnected-(U6B-PT27A/+/PCLKT0_1-PadC7)
- U6 pad C8: /IO62 -> /IFCLK
- U6 pad C9: /IO11 -> unconnected-(U6C-PT38B/-/GR_PCLK1_1-PadC9)
- U6 pad D1: /IO54 -> /IO20
- U6 pad D10: /IO30 -> unconnected-(U6C-PT47A/+-PadD10)
- U6 pad D11: /IO29 -> unconnected-(U6C-PT51A/+-PadD11)
- U6 pad D2: /IO53 -> GND
- U6 pad D3: /IO43 -> unconnected-(U6G-PL2D/-/LDQ8-PadD3)
- U6 pad D4: +1V2 -> unconnected-(U6B-PT9B/--PadD4)
- U6 pad D5: /IO63 -> unconnected-(U6B-PT13B/--PadD5)
- U6 pad D6: +3V3 -> unconnected-(U6B-PT20B/--PadD6)
- U6 pad D7: /IO09 -> unconnected-(U6B-PT24B/-/GR_PCLK0_0-PadD7)
- U6 pad D8: +1V2 -> unconnected-(U6C-PT33B/-/PCLKC1_1-PadD8)
- U6 pad D9: /IO15 -> unconnected-(U6C-PT40A/+-PadD9)
- U6 pad E1: /IO32 -> /IO23
- U6 pad E11: /IO31 -> unconnected-(U6C-PT51B/--PadE11)
- U6 pad E2: /IO55 -> /IO21
- U6 pad E3: /IO44 -> unconnected-(U6G-PL5C/+/LDQ8-PadE3)
- U6 pad E4: +3V3 -> unconnected-(U6B-PT9A/+-PadE4)
- U6 pad E5: GND -> unconnected-(U6B-PT13A/+-PadE5)
- U6 pad E6: GND -> unconnected-(U6B-PT20A/+-PadE6)
- U6 pad E7: GND -> unconnected-(U6B-PT24A/+/GR_PCLK0_1-PadE7)
- U6 pad E8: /IO17 -> unconnected-(U6C-PT33A/+/PCLKT1_1-PadE8)
- U6 pad E9: /IO16 -> unconnected-(U6C-PT40B/--PadE9)
- U6 pad F1: /IO34 -> /IO24
- U6 pad F10: /IO22 -> +3V3
- U6 pad F11: unconnected-(U6B-IOR_140_GBIN3-PadF11) -> +3V3
- U6 pad F2: /IO33 -> /IO22
- U6 pad F4: /IO45 -> unconnected-(U6G-PL8C/+/LDQ8-PadF4)
- U6 pad F5: GND -> unconnected-(U6G-PL8D/-/LDQ8-PadF5)
- U6 pad F6: GND -> +3V3
- U6 pad F7: GND -> +3V3
- U6 pad F8: +3V3 -> GND
- U6 pad F9: /IO23 -> GND
- U6 pad G1: unconnected-(U6D-IOL_14A_GBIN6-PadG1) -> /IO26
- U6 pad G10: /IO27 -> GND
- U6 pad G11: /IO28 -> +2V5
- U6 pad G2: /IO35 -> /IO25
- U6 pad G3: /IO46 -> unconnected-(U6G-PL14C/+/VREF1_7/LDQ20-PadG3)
- U6 pad G4: +3V3 -> unconnected-(U6G-PL11B/-/HS/LDQ8-PadG4)
- U6 pad G5: GND -> unconnected-(U6G-PL11A/+/HS/LDQ8-PadG5)
- U6 pad G6: GND -> +1V1
- U6 pad G7: GND -> +1V1
- U6 pad G8: /IO18 -> GND
- U6 pad G9: /IO19 -> +1V1
- U6 pad H1: /IO40 -> GND
- U6 pad H10: /IO25 -> GND
- U6 pad H11: /IO26 -> +3V3
- U6 pad H2: /IO36 -> /IO27
- U6 pad H3: /IO47 -> unconnected-(U6G-PL14D/-/LDQ20-PadH3)
- U6 pad H4: +1V2 -> unconnected-(U6G-PL17B/-/HS/LDQ20-PadH4)
- U6 pad H5: GND -> unconnected-(U6G-PL17A/+/HS/LDQ20-PadH5)
- U6 pad H7: /CTL0/FLAGA -> +3V3
- U6 pad H8: +1V2 -> GND
- U6 pad H9: /CTL1/FLAGB -> GND
- U6 pad J1: /IO37 -> /IO28
- U6 pad J10: /IO20 -> GND
- U6 pad J11: /IO24 -> +3V3
- U6 pad J2: /IO41 -> /IO29
- U6 pad J3: /PA5/FIOADDR1 -> unconnected-(U6G-PL20C/+/GR_PCLK7_0/LDQ20-PadJ3)
- U6 pad J4: /PA6/PKTEND -> unconnected-(U6G-PL17C/+/LDQ20-PadJ4)
- U6 pad J5: /PA4/FIOADDR0 -> unconnected-(U6G-PL17D/-/LDQ20-PadJ5)
- U6 pad J6: Net-(U6E-VCCPLL0) -> +3V3
- U6 pad J7: /PA0/~{INT0} -> +3V3
- U6 pad J8: /PA2/SLOE -> GND
- U6 pad J9: /IOB_106_SDI -> GND
- U6 pad K1: /IO39 -> /IO30
- U6 pad K10: /IOB_108_SS -> GND
- U6 pad K11: /IO21 -> +3V3
- U6 pad K2: /IO38 -> /IO31
- U6 pad K3: /PB7/FD7 -> unconnected-(U6G-PL20D/-/LDQ20-PadK3)
- U6 pad K4: /PB5/FD5 -> unconnected-(U6F-PL29A/+/GR_PCLK6_0/HS/LDQ32-PadK4)
- U6 pad K5: /PB3/FD3 -> unconnected-(U6F-PL29B/-/HS/LDQ32-PadK5)
- U6 pad K6: /IFCLK -> GND
- U6 pad K7: /PB1/FD1 -> GND
- U6 pad K8: /CDONE -> GND
- U6 pad K9: /IOB_105_SDO -> GND
- U6 pad L1: /RDY1/SLWR -> /IO00
- U6 pad L10: /IOB_107_SCK -> +1V1
- U6 pad L2: /RDY0/SLRD -> /IO01
- U6 pad L3: /PB6/FD6 -> unconnected-(U6F-PL32C/+/LDQ32-PadL3)
- U6 pad L4: /PB4/FD4 -> unconnected-(U6F-PL29C/+/GR_PCLK6_1/LDQ32-PadL4)
- U6 pad L5: /CLKOUT -> unconnected-(U6F-PL29D/-/LDQ32-PadL5)
- U6 pad L6: Net-(U6E-GNDPLL0) -> +3V3
- U6 pad L7: /PB2/FD2 -> +2V5
- U6 pad L8: /PB0/FD0 -> +1V1
- U6 pad L9: /~{CRESET} -> +1V1
- U7 pad 1: /IOB_108_SS -> /SPI_CS
- U7 pad 2: /IOB_106_SDI -> /SPI_MISO
- U7 pad 3: Net-(U7-IO2) -> /SPI_D2
- U7 pad 5: /IOB_105_SDO -> /SPI_MOSI
- U7 pad 6: /IOB_107_SCK -> /SPI_CLK
- U7 pad 7: Net-(U7-IO3) -> /SPI_D3
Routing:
- net +1V2: track 94.2 -> 0.00 mm, vias 8 -> 0
- net +3V3: track 142.5 -> 84.4 mm, vias 22 -> 23
- net /~{CRESET}: track 53.9 -> 0.97 mm, vias 5 -> 0
- net /IO23: track 42.8 -> 2.66 mm
- net /IOB_105_SDO: track 39.8 -> 0.00 mm, vias 2 -> 0
- net /IOB_107_SCK: track 37.5 -> 0.00 mm, vias 2 -> 0
- net /IO22: track 38.8 -> 3.63 mm
- net /IO28: track 35.8 -> 1.59 mm
- net /IOB_108_SS: track 34.1 -> 0.00 mm, vias 3 -> 0
- net /IOB_106_SDI: track 31.6 -> 0.00 mm, vias 2 -> 0
- net /IO27: track 33.4 -> 2.46 mm
- net /IO00: track 32.4 -> 2.06 mm
- net /IO47: track 33.0 -> 3.30 mm, vias 1 -> 0
- net /IO09: track 42.3 -> 13.6 mm
- net /IO08: track 43.9 -> 15.6 mm
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- added copper zone on B.Cu, net GND
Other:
- board text added: "3.3V TMS GND TCK"
- board text added: "TDI TDO"
- board text removed: "3.3V GND GND GND"
- board text removed: "CS SCK MOSI MISO RST"

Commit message: Save
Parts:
- added C46: 4.7u, Capacitor_SMD:C_0402_1005Metric, B.Cu at (159.5, 84.9)
- added C47: 4.7u, Capacitor_SMD:C_0402_1005Metric, B.Cu at (160.8, 76.5)
- moved C32 72.0 mm to (123.0, 88.0), turned to 180 degrees
- moved C24 69.6 mm to (125.4, 86.7), turned to 180 degrees
- moved R82 69.3 mm to (123.0, 87.0)
- moved C23 68.0 mm to (119.6, 98.3)
- moved C28 68.0 mm to (111.5, 88.5)
- moved R81 67.4 mm to (123.0, 89.0), turned to 180 degrees
- moved U8 60.9 mm to (125.4, 88.4), turned to 180 degrees
- moved C34 58.7 mm to (125.3, 90.2), turned to 180 degrees
- moved C33 56.6 mm to (125.3, 91.7), turned to 180 degrees
- moved L1 56.5 mm to (128.1, 88.3), turned to -90 degrees
- moved U2 56.3 mm to (117.8, 93.7)
- moved C31 51.7 mm to (132.2, 87.6)
- moved U1 9.35 mm to (132.3, 85.5), turned to 90 degrees
- moved C3 9.14 mm to (130.5, 85.5), turned to -90 degrees
- moved FB1 8.05 mm to (115.7, 82.1)
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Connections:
- U5 pad 34: /~{CRESET} -> /PROGRAMN
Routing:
- net /PROGRAMN: track 3.38 -> 45.6 mm, vias 1 -> 2
- net +1V1: track 6.30 -> 46.2 mm
- net /CDONE: track 8.80 -> 45.4 mm, vias 2 -> 4
- net /IO00: track 2.06 -> 30.3 mm
- net /IO56: track 4.44 -> 32.6 mm
- net /IO08: track 15.6 -> 43.2 mm
- net /IO28: track 1.59 -> 28.5 mm
- net /IO09: track 13.6 -> 40.1 mm
- net /IO01: track 3.03 -> 28.5 mm
- net /IO57: track 3.23 -> 28.6 mm
- net /IO27: track 2.46 -> 27.7 mm
- net /IO48: track 14.9 -> 39.4 mm
- net /IO39: track 12.3 -> 36.0 mm
- net /IO49: track 15.8 -> 39.0 mm
- net /IO26: track 1.59 -> 23.8 mm
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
